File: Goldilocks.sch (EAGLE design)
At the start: 68 parts, among them IC1 ATMEGA1284P, IC2 ATMEGA16U2-MU, IC3 MC33269DT-5.0, IC4 LM358D, IC5 LP2985-33DBVR, J1 Power, J2 Analog, J3 Digital_8_13, J4 Digital_0_7, J5 DC_2_1MM, P1 USB-6PSMT, P2 ICSP:MAIN, P3 ICSP:USB, P4 microSD, P5V M01SMD, Q1 FDN340P, Q2 2N7002, X1 20MHz, X2 16MHz

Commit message: Routing
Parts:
- removed C1: 47uF 25V, rcl:CPOL-EUD
- removed C11: 100nF 0603, freetronics:CAP0603
- removed IC3: MC33269DT-5.0, linear:MC33269D-5.0
- removed IC4: LM358D, linear:LM358D
- removed P5V, PGND: M01SMD, freetronics:M01SMD
- removed Q1: FDN340P, freetronics-master-v1:MOSFET-PCHANNEL
- removed R8, R9: 10K 0603, freetronics:RESISTOR0603
- removed RN6: 1K, freetronics-master-v1:4R-NCAY16
- removed RN8: 2K2, freetronics-master-v1:4R-NCAY16
- removed S1: RESET, freetronics:TAC_SWITCHSMD
- added C15: 10nF 50V 0402, freetronics-jon:C-EU0402C
- added C16: 22pF NOT PLACED, freetronics-jon:C-EU0402C
- added C17: 2.2nF 0402, freetronics-jon:C-EU0402C
- added C18: 100nF 0402, freetronics-jon:C-EU0402C
- added C19: 10uF 50V 1210 ceramic, freetronics-jon:C-EUC1210
- added C20: (no value), freetronics-jon:C-EUC1210
- added J10, J8: Power, freetronics:M08
- added J11: AREF, freetronics-2:M01PTH
- added J13, J6, J7: Digital_0_7, freetronics:M08
- added J9: Analog, freetronics:M06SIP
- added JP1: (no value), freetronics-master-v1.1:M02PTH
- added JP2: (no value), freetronics-master-v1.1:M03PTH
- added Q3: (no value), freetronics-original:CRYSTALTC38H
- added R16, R17, R18: 1K 0402, freetronics-jon:RESISTOR0402
- added R19, R20, R21: 2K2 0402, freetronics-jon:RESISTOR0402
- added R22: 100K 0402, freetronics-jon:RESISTOR0402
- added R23: 53.6K 1% 0402, freetronics-jon:RESISTOR0402
- added R24: 15K 0402, freetronics-jon:RESISTOR0402
- added R25: 10K 1% 0402, freetronics-jon:RESISTOR0402
- added U$15, U$19, U$20, U$21, U$22, U$23, U$24, U$25, U$27, U$29, U$30, U$31, U$32, U$33, U$34, U$35, U$36, U$37, U$38, U$39, U$40, U$41, U$43, U$44: SJC0402, freetronics-jon:SJC0402
- added U$26, U$28: TAC-SWITCH-3PIN-GND, freetronics-jon:TAC-SWITCH-3PIN-GND
- added U$4: EUP3476SO08T, freetronics-jon:EUP3476SO08T
- added U$42: MOSI, freetronics-jon:SJ0402O
- added U$45: CDRH6D38SMT, freetronics-jon:CDRH6D38SMT
- added U$46: SCK, freetronics-jon:SJ0402O
- added U$47, U$48, U$49, U$50: (no value), freetronics-jon:SJ0402O
- added U$7: JTAG2MM, freetronics-jon:JTAG2MM
- added U$8: MISO, freetronics-jon:SJ0402O
- C10, C29, C4, C8, C9: value 100nF 0603 -> 100nF 0402; device freetronics:CAP0603 -> freetronics-jon:C-EU0402C
- C12, C13, C2, C3: value 22pF 0603 -> 22pF 0402; device freetronics:CAP0603 -> freetronics-jon:C-EU0402C
- C14: device freetronics:CAP0603 -> freetronics-jon:C-EU0402C
- C6, C7: value 1uF 0603 -> 1uF 0402; device freetronics:CAP0603 -> freetronics-jon:C-EU0402C
- IC2: value ATMEGA16U2-MU -> ATMEGA32U2-MU
- J2: value Analog -> Digital_0_7; device freetronics:M06SIP -> freetronics:M08
- LED1, LED2, LED3, LED4: device freetronics:LED0603 -> freetronics-jon:LED0402
- R1, R11: value 10K 0603 -> 10K 0402; device freetronics:RESISTOR0603 -> freetronics-jon:RESISTOR0402
- R10, R2, R3, R4, R5, R7: value 1K 0603 -> 1K 0402; device freetronics:RESISTOR0603 -> freetronics-jon:RESISTOR0402
- R12: device freetronics:RESISTOR0603 -> freetronics-jon:RESISTOR0402
- R13: value 27R 0603 -> 27R 0402; device freetronics:RESISTOR0603 -> freetronics-jon:RESISTOR0402
- R14, R15: value 22R 0603 -> 22R 0402; device freetronics:RESISTOR0603 -> freetronics-jon:RESISTOR0402
- R6: value 1M 0603 -> 1M 0402; device freetronics:RESISTOR0603 -> freetronics-jon:RESISTOR0402
- SJ1, SJ2: device jumper:SJ -> freetronics-jon:SJCN
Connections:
- removed net A4_SDA: J2.5
- removed net A5_SCL: J2.6
- removed net DTR: IC2.(CTS)PD7, SJ1.1, SJ3.2
- removed net MISO2: IC2.(MISO)PB3, P3.1
- removed net MOSI2: IC2.(MOSI)PB2, P3.4
- removed net N$10: IC4A.OUT, IC4B.+IN
- removed net N$12: IC4B.-IN, IC4B.OUT, Q1.G
- removed net N$9: IC4A.+IN, R8.1, R9.2
- removed net SCK2: IC2.(SCLK)PB1, P3.3
- removed net SS2: IC2.(SS)PB0
- new net 2_MISO: IC2.(MISO)PB3, J13.4, P3.1, U$8.1
- new net 2_MOSI: IC2.(MOSI)PB2, J13.3, P3.4, U$42.1
- new net 2_PB4: IC2.PB4, J13.5
- new net 2_PB5: IC2.PB5, J13.6
- new net 2_PB6: IC2.PB6, J13.7
- new net 2_PB7: IC2.PB7, J13.8
- new net 2_PD0: IC2.PD0, J6.1
- new net 2_PD1: IC2.PD1, J6.2
- new net 2_PD4: IC2.PD4, J6.5, U$44.1
- new net 2_PD5: IC2.(XCK)PD5, J6.6, U$43.1
- new net 2_PD6: IC2.(RTS)PD6, J6.7, U$48.1
- new net 2_PD7: IC2.(CTS)PD7, J6.8, SJ1.1, SJ3.2
- new net 2_SCK: IC2.(SCLK)PB1, J13.2, P3.3, U$46.1
- new net 2_SS: IC2.(SS)PB0, J13.1, U$47.1, U$49.1, U$50.1
- new net 5V_PSU: C20.1, JP2.3, R23.2, U$45.2
- new net A0_H: J10.1, J9.1, U$15.1
- new net A1_H: J10.2, J9.2, U$19.1
- new net A2_H: J10.3, J9.3, U$20.1
- new net A3_H: J10.4, J9.4, U$21.1
- new net A4_H: J10.5, J9.5, U$22.1
- new net A5_H: J10.6, J9.6, U$23.1
- new net A6_H: J10.7, JP1.2, U$24.1
- new net A7_H: J10.8, JP1.1, U$25.1
- new net AVCC: IC1.AVCC
- new net D0_RX_H: J4.1, J7.1, U$27.1
- new net D10_H: J2.5, J3.3, U$38.1
- new net D11_MOSI_H: J2.6, J3.4, U$39.1
- new net D12_MISO_H: J2.7, J3.5, U$40.1
- new net D13_SCK_H: J2.8, J3.6, U$41.1
- new net D1_TX_H: J4.2, J7.2, U$29.1
- new net D2_H: J4.3, J7.3, U$30.1
- new net D3_H: J4.4, J7.4, U$31.1
- new net D4_H: J4.5, J7.5, U$32.1
- new net D5_H: J4.6, J7.6, U$33.1
- new net D6_H: J4.7, J7.7, U$34.1
- new net D7_H: J4.8, J7.8, U$35.1
- new net D8_H: J2.3, J3.1, U$36.1
- new net D9_H: J2.4, J3.2, U$37.1
- new net N$19: IC1.PC6(TOSC1/PCINT22), Q3.2
- new net N$22: IC1.PC7(TOSC2/PCINT23), Q3.1
- new net N$23: C15.2, U$4.BS
- new net N$25: C15.1, U$4.SW, U$45.1
- new net N$28: C17.1, R24.1
- new net N$31: R23.1, R25.2, U$4.FB
- new net N$34: C18.1, U$4.SS
- new net N$37: R22.2, U$4.EN
- new net N$43: C16.1, R24.2, U$4.COMP
- new net NC: J1.1, J8.1
- new net PB0: IC1.PB0(PCINT8/XCK0/T0), J2.1
- new net PB1: IC1.PB1(PCINT9/CLKO/T1), J2.2
- new net VREF: U$7.4
- net 3V3: now also J8.4; no longer IC4A.-IN
- net 5V: now also J8.2, J8.5, JP2.2; no longer C11.1, IC3.VO, IC4P.V+, P5V.1, Q1.S
- net A0: now also U$15.2; no longer J2.1
- net A1: now also U$19.2; no longer J2.2
- net A2: now also U$20.2; no longer J2.3
- net A3: now also U$21.2; no longer J2.4
- net A4: now also U$22.2
- net A5: now also U$23.2
- net A6: now also U$24.2
- net A7: now also U$25.2
- net AREF: now also IC1.AREF, J11.1
- net D0_RX: now also U$27.2; no longer J4.1
- net D10: now also U$38.2, U$48.2, U$49.2; no longer J3.3
- net D11_MOSI: now also R17.2, U$39.2, U$42.2; no longer J3.4, RN6C.2
- net D12_MISO: now also U$40.2, U$8.2; no longer J3.5
- net D13_SCK: now also R18.2, U$41.2, U$46.2; no longer J3.6, RN6B.2
- net D1_TX: now also U$29.2; no longer J4.2
- net D2: now also U$30.2; no longer J4.3
- net D3: now also U$31.2; no longer J4.4
- net D4: now also R16.2, U$32.2; no longer J4.5, RN6D.2
- net D5: now also U$33.2; no longer J4.6
- net D6: now also U$34.2; no longer J4.7
- net D7: now also U$35.2; no longer J4.8
- net D8: now also U$36.2, U$50.2; no longer J3.1
- net D9: now also U$37.2; no longer J3.2
- net GND: now also C16.2, C17.2, C18.2, C19.2, C20.2, J8.6, J8.7, R19.1, R20.1, R21.1, R25.1, U$26.1, U$26.3, U$26.GND@1, U$26.GND@2, U$28.1, U$28.3, U$28.GND@1, U$28.GND@2, U$4.GND, U$4.TGND, U$7.10, U$7.2; no longer C1.-, C11.2, IC3.ADJ, IC4P.V-, PGND.1, R9.1, RN8A.1, RN8B.1, RN8C.1, S1.1, S1.2
- net N$118: now also R16.1, R21.2; no longer RN6D.1, RN8A.2
- net N$119: now also R17.1, R20.2; no longer RN6C.1, RN8C.2
- net N$120: now also R18.1, R19.2; no longer RN6B.1, RN8B.2
- net RESET: now also J8.3, U$26.2, U$47.2, U$7.6; no longer S1.3, S1.4
- net RESET2: now also U$28.2
- net RXLED: now also U$44.2; no longer IC2.PD4
- net TCK: now also U$7.1
- net TDI: now also U$7.9
- net TDO: now also U$7.3
- net TMS: now also U$7.5
- net TXLED: now also U$43.2; no longer IC2.(XCK)PD5
- net USBRXD: now also J6.4
- net USBTXD: now also J6.3
- net USBVCC: now also JP2.1; no longer Q1.D
- net VIN: now also C19.1, J8.8, R22.1, U$4.IN; no longer C1.+, IC3.VI, R8.2
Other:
- note added: "ATmega32U2 Microcontroller"
- note removed: "ATmega16U2 Microcontroller"
- note removed: "DCInput/USBVCC Auto-switch"
- note removed: "NOTE: reconnect across RESET-EN and GROUND after other routing is done"
- note removed: "Prototyping Area"
- moved on the sheet: C10, C12, C13, C2, C29, C3, C4, C5, C7, C8, C9, D1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

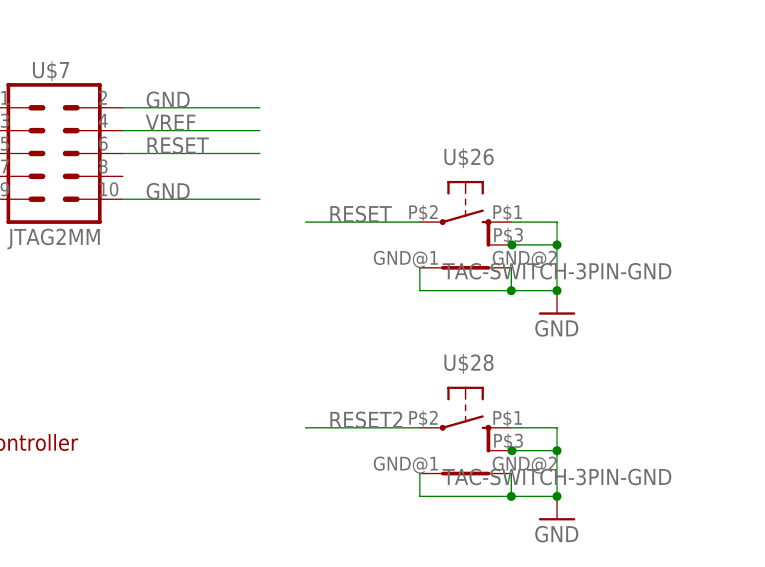
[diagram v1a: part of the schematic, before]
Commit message: Switched to 4 layer PCB
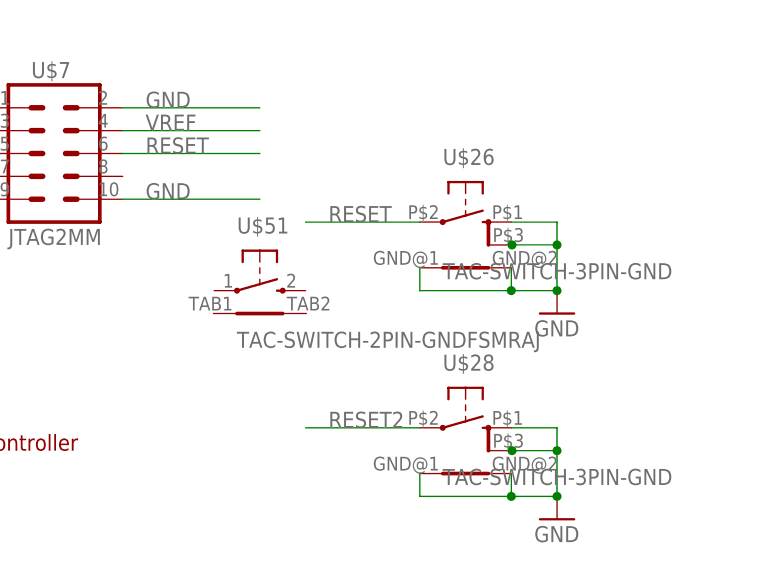
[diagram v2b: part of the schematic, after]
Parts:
- added U$51: TAC-SWITCH-2PIN-GNDFSMRAJ, freetronics-jon:TAC-SWITCH-2PIN-GNDFSMRAJ
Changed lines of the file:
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@@
 <part name="U$49" library="freetronics-jon" deviceset="SJ" device="0402O"/>
 <part name="U$50" library="freetronics-jon" deviceset="SJ" device="0402O"/>
+<part name="U$51" library="freetronics-jon" deviceset="TAC-SWITCH-2PIN-GND" device="FSMRAJ"/>
 </parts>
 <sheets>
@@
 <attribute name="NAME" x="116.84" y="320.04" size="1.778" layer="95"/>
 </instance>
+<instance part="U$51" gate="G$1" x="195.58" y="330.2"/>
 </instances>
 <busses>

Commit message: Hopefully ready for v1.0 release
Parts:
- removed IC5: LP2985-33DBVR, freetronics-jon:TEXAS_TPS77033
- removed J13, J6: Digital_0_7, freetronics:M08
- removed J5: DC_2_1MM, freetronics:POWER_JACKPTH
- removed JP2: (no value), freetronics-master-v1.1:M03PTH
- removed U$15, U$19, U$20, U$21, U$22, U$23, U$24, U$25, U$27, U$29, U$30, U$31, U$32, U$33, U$34, U$35, U$36, U$37, U$38, U$39, U$40, U$41, U$43, U$44: SJC0402, freetronics-jon:SJC0402
- removed U$42: MOSI, freetronics-jon:SJ0402O
- removed U$46: SCK, freetronics-jon:SJ0402O
- removed U$47, U$48, U$49, U$50: (no value), freetronics-jon:SJ0402O
- removed U$51: TAC-SWITCH-2PIN-GNDFSMRAJ, freetronics-jon:TAC-SWITCH-2PIN-GNDFSMRAJ
- removed U$7: JTAG2MM, freetronics-jon:JTAG2MM
- removed U$8: MISO, freetronics-jon:SJ0402O
- removed X1: 20MHz, freetronics-master-v1:CRYSTALHC49UV
- removed X2: 16MHz, freetronics-master-v1:CRYSTALHC49UV
- added C1, C11: 22pF 0603, freetronics-jon:C-EUC0603K
- added C21: 100nF 0402, freetronics-jon:C-EU0402C
- added H1: Power, freetronics:M08
- added H13: 32U2_PB, freetronics:M08
- added H14: 32U2 PD, freetronics:M08
- added H15: (no value), freetronics-master-v1.1:M03PTH
- added H7: JTAG2MM, freetronics-jon:JTAG2MM
- added IC4: LP2985-33DBVR, freetronics-jon:TEXAS_TPS77033
- added L2: 0805 INDUCTOR, freetronics-master-v1:INDUCTOR0805-LARGE
- added SJ10, SJ11, SJ12, SJ13, SJ16, SJ17, SJ18, SJ19, SJ20, SJ21, SJ22, SJ23, SJ24, SJ25, SJ26, SJ27, SJ28, SJ29, SJ4, SJ5, SJ6, SJ7, SJ8, SJ9: SJC0402, freetronics-jon:SJC0402
- added SJ14, SJ15, SJ33, SJ34, SJ35, SJ36: (no value), freetronics-jon:SJ0402O
- added SJ30: MISO, freetronics-jon:SJ0402O
- added SJ31: MOSI, freetronics-jon:SJ0402O
- added SJ32: SCK, freetronics-jon:SJ0402O
- added XTL1: 20MHz, freetronics-jon:CRYSTALHC49UV
- added XTL2: 16MHz, freetronics-jon:CRYSTALHC49UV
- D1: device freetronics:DIODESMB -> freetronics-jon:DIODESMB
- H10: value (none) -> AnalogB
- H11: value Digital_0_7 -> Digital_8_13B
- H12: value Digital_0_7 -> Digital_0_7B
- H2: value Power -> Analog
- H8: value Power -> PowerB
- H9: value Analog -> AnalogB
- J1: value Power -> DC_2_1MM; device freetronics:M08 -> freetronics:POWER_JACKPTH
- renumbered CD to JP3, J10 to H2, J2 to H11, J3 to H3, J4 to H4, J7 to H12, J8 to H8, J9 to H9, JP1 to H10, P2 to H5, P3 to H6, Q2 to Q1, Q3 to XTL3, U$26 to SW1, U$28 to SW2, U$4 to IC3, U$45 to L3
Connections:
- removed net 3V3: C7.2, H8.4, IC5.OUT, J1.4
- removed net 3V3D: C29.1, P4.VCC
- new net 3.3V: C29.1, C7.2, H1.4, H8.4, IC4.OUT, P4.VCC
- net 2_MISO: now also H13.4, SJ30.1; no longer J13.4, U$8.1
- net 2_MOSI: now also H13.3, SJ31.1; no longer J13.3, U$42.1
- net 2_PB4: now also H13.5; no longer J13.5
- net 2_PB5: now also H13.6; no longer J13.6
- net 2_PB6: now also H13.7; no longer J13.7
- net 2_PB7: now also H13.8; no longer J13.8
- net 2_PD0: now also H14.1; no longer J6.1
- net 2_PD1: now also H14.2; no longer J6.2
- net 2_PD4: now also H14.5, SJ13.1; no longer J6.5, U$44.1
- net 2_PD5: now also H14.6, SJ12.1; no longer J6.6, U$43.1
- net 2_PD6: now also H14.7, SJ33.1; no longer J6.7, U$48.1
- net 2_PD7: now also H14.8; no longer J6.8
- net 2_SCK: now also H13.2, SJ32.1; no longer J13.2, U$46.1
- net 2_SS: now also H13.1, SJ34.1, SJ35.1, SJ36.1; no longer J13.1, U$47.1, U$49.1, U$50.1
- net 5V: now also H1.2, H1.5, H15.2, IC4.!EN, IC4.IN, L2.2; no longer IC5.!EN, IC5.IN, J1.2, J1.5, JP2.2
- net 5V_PSU: now also H15.3; no longer JP2.3
- net A0: now also SJ4.2; no longer U$15.2
- net A0_H: now also SJ4.1; no longer U$15.1
- net A1: now also SJ5.2; no longer U$19.2
- net A1_H: now also SJ5.1; no longer U$19.1
- net A2: now also SJ6.2; no longer U$20.2
- net A2_H: now also SJ6.1; no longer U$20.1
- net A3: now also SJ7.2; no longer U$21.2
- net A3_H: now also SJ7.1; no longer U$21.1
- net A4: now also SJ8.2; no longer U$22.2
- net A4_H: now also SJ15.2, SJ8.1; no longer U$22.1
- net A5: now also SJ9.2; no longer U$23.2
- net A5_H: now also SJ14.2, SJ9.1; no longer U$23.1
- net A6: now also SJ10.2; no longer U$24.2
- net A6_H: now also SJ10.1; no longer U$24.1
- net A7: now also SJ11.2; no longer U$25.2
- net A7_H: now also SJ11.1; no longer U$25.1
- net AVCC: now also C21.1, L2.1
- net D0_RX: now also SJ16.2; no longer U$27.2
- net D0_RX_H: now also SJ16.1; no longer U$27.1
- net D10: now also SJ26.2, SJ33.2, SJ34.2; no longer U$38.2, U$48.2, U$49.2
- net D10_H: now also SJ26.1; no longer U$38.1
- net D11_MOSI: now also SJ27.2, SJ31.2; no longer U$39.2, U$42.2
- net D11_MOSI_H: now also SJ27.1; no longer U$39.1
- net D12_MISO: now also SJ28.2, SJ30.2; no longer U$40.2, U$8.2
- net D12_MISO_H: now also SJ28.1; no longer U$40.1
- net D13_SCK: now also SJ29.2, SJ32.2; no longer U$41.2, U$46.2
- net D13_SCK_H: now also SJ29.1; no longer U$41.1
- net D1_TX: now also SJ17.2; no longer U$29.2
- net D1_TX_H: now also SJ17.1; no longer U$29.1
- net D2: now also SJ18.2; no longer U$30.2
- net D2_H: now also SJ18.1; no longer U$30.1
- net D3: now also SJ19.2; no longer U$31.2
- net D3_H: now also SJ19.1; no longer U$31.1
- net D4: now also SJ20.2; no longer U$32.2
- net D4_H: now also SJ20.1; no longer U$32.1
- net D5: now also SJ21.2; no longer U$33.2
- net D5_H: now also SJ21.1; no longer U$33.1
- net D6: now also SJ22.2; no longer U$34.2
- net D6_H: now also SJ22.1; no longer U$34.1
- net D7: now also SJ23.2; no longer U$35.2
- net D7_H: now also SJ23.1; no longer U$35.1
- net D8: now also SJ24.2, SJ35.2; no longer U$36.2, U$50.2
- net D8_H: now also SJ24.1; no longer U$36.1
- net D9: now also SJ25.2; no longer U$37.2
- net D9_H: now also SJ25.1; no longer U$37.1
- net GND: now also C1.2, C11.2, C21.2, H1.6, H1.7, H7.10, H7.2, IC4.GND, J1.GND, J1.GNDBREAK; no longer IC5.GND, J1.6, J1.7, J5.GND, J5.GNDBREAK, U$7.10, U$7.2
- net N$113: now also XTL2.2; no longer X2.2
- net N$114: now also XTL2.1; no longer X2.1
- net N$19: now also C1.1
- net N$22: now also C11.1
- net N$5: now also XTL1.2; no longer X1.2
- net N$7: now also XTL1.1; no longer X1.1
- net N$8: now also J1.PWR; no longer J5.PWR
- net NC: now also H1.1; no longer J1.1
- net RESET: now also H1.3, H7.6, SJ36.2; no longer J1.3, U$47.2, U$7.6
- net RXLED: now also SJ13.2; no longer U$44.2
- net SCL: now also SJ14.1
- net SDA: now also SJ15.1
- net TCK: now also H7.1; no longer U$7.1
- net TDI: now also H7.9; no longer U$7.9
- net TDO: now also H7.3; no longer U$7.3
- net TMS: now also H7.5; no longer U$7.5
- net TXLED: now also SJ12.2; no longer U$43.2
- net USBRXD: now also H14.4; no longer J6.4
- net USBTXD: now also H14.3; no longer J6.3
- net USBVCC: now also H15.1; no longer JP2.1
- net VIN: now also H1.8; no longer J1.8
- net VREF: now also H7.4; no longer U$7.4
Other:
- note added: "1284P ICSP Header"
- note added: "32U2 Breakouts"
- note added: "32u2 ICSP Header"
- note added: "Analog Header Isolation"
- note added: "Digital Header Isolation"
- note added: "Header Breakouts"
- note added: "I2C/A4-5 Cross Link"
- note added: "SPI Cross Link"
- note added: "SS/RESET Cross Link"
- note added: "Shield Headers"
- note added: "TX/RX LED Isolation"
- note added: "V1.0 (2013-05-03)"
- note removed: "V1.0 (2013-03-18)"
- moved on the sheet: C10, C4, C5, C7, C8, LED4, R1, R10, R4, R5, SJ1, SJ3

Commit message: v1.1 release for production
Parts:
- added C23, C24, C25: 100nF 0402, freetronics-jon:C-EU0402C
- added JP1: (no value), freetronics-master-v1.1:M04PTH
- added R26, R8, R9: 1K 0402, freetronics-jon:RESISTOR0402
- C1, C11: value 22pF 0603 -> 15pF 0402; device freetronics-jon:C-EUC0603K -> freetronics-jon:C-EU0402C
- C14: value 100nF 0603 -> 100nF 0402
- C20: value (none) -> 22uF 10V 1210 ceramic
- H14: value 32U2 PD -> 32U2_PD
- R12: value 1M 0603 -> 1M 0402
- SJ14, SJ15: device freetronics-jon:SJ0402O -> freetronics-master-v1.1:SJ
- SJ30, SJ31, SJ32, SJ33, SJ34, SJ35, SJ36: device freetronics-jon:SJ0402O -> freetronics-jon:SJN
- SW1, SW2: value TAC-SWITCH-3PIN-GND -> TAC-SWITCH-1TAB; device freetronics-jon:TAC-SWITCH-3PIN-GND -> freetronics-jon:TAC-SWITCH-1TAB
- renumbered C29 to C22, J11 to H16, JP3 to H17
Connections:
- new net N$24: R9.1, SJ31.2
- new net N$36: R26.1, SJ32.2
- new net N$9: R8.1, SJ30.2
- net 5V: now also C24.1, C25.1, JP1.2
- net AVCC: now also C23.1
- net D11_MOSI: now also R9.2; no longer SJ31.2
- net D12_MISO: now also R8.2; no longer SJ30.2
- net D13_SCK: now also R26.2; no longer SJ32.2
- net GND: now also C23.2, C24.2, C25.2, JP1.1, SW1.2, SW2.2; no longer SW1.1, SW1.GND@1, SW1.GND@2, SW2.1, SW2.GND@1, SW2.GND@2
- net RESET: now also SW1.1; no longer SW1.2
- net RESET2: now also SW2.1; no longer SW2.2
- net SCL: now also JP1.3
- net SDA: now also JP1.4
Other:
- note added: "17/18"
- note added: "27/28"
- note added: "38/39"
- note added: "Place near pins:"
- moved on the sheet: H13, H14
